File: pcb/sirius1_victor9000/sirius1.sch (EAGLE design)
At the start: 28 parts, among them IC3 STM32F042F4, SW1 324_SW, SW4 324_SW, U1 RJ45

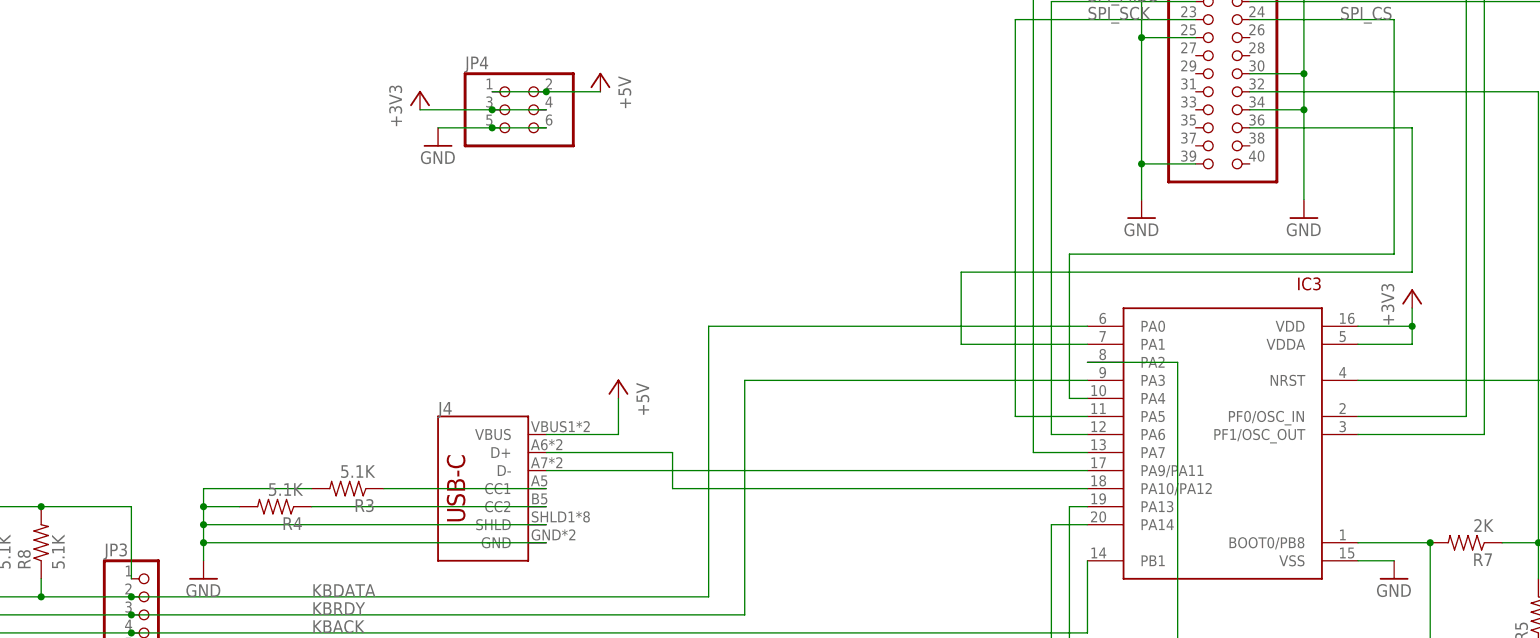
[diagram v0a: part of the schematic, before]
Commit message: added presence detection
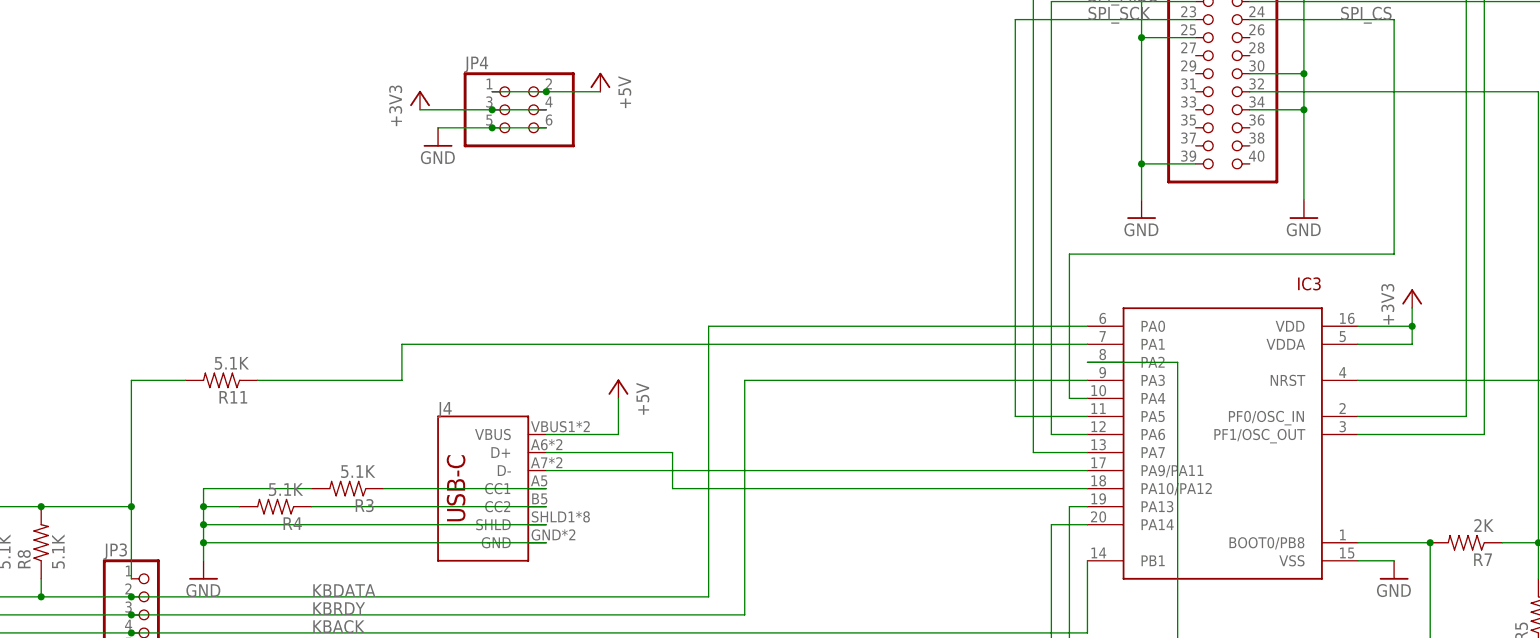
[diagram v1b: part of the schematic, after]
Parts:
- added R11: 5.1K, SparkFun-Passives:RESISTOR0805-RES
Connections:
- removed net N$12: IC3.PA1, JP1.36
- new net N$4: IC3.PA1, R11.1
- net N$27: now also R11.2
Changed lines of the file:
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@@
 <part name="JP3" library="pinhead" library_urn="urn:adsk.eagle:library:325" deviceset="PINHD-1X5" device="" package3d_urn="urn:adsk.eagle:package:22469/2"/>
 <part name="GND13" library="supply1" library_urn="urn:adsk.eagle:library:371" deviceset="GND" device=""/>
+<part name="R11" library="SparkFun-Passives" deviceset="RESISTOR" device="0805-RES" value="5.1K"/>
 </parts>
 <sheets>
@@
 <instance part="GND13" gate="1" x="-53.34" y="-142.24" smashed="yes">
 <attribute name="VALUE" x="-55.88" y="-144.78" size="1.778" layer="96"/>
+</instance>
+<instance part="R11" gate="G$1" x="-40.64" y="-96.52" smashed="yes" rot="R180">
+<attribute name="NAME" x="-36.83" y="-98.0186" size="1.778" layer="95" rot="R180"/>
+<attribute name="VALUE" x="-36.83" y="-93.218" size="1.778" layer="96" rot="R180"/>
 </instance>
 </instances>
@@
 </segment>
 </net>
-<net name="N$12" class="0">
-<segment>
-<pinref part="IC3" gate="G$1" pin="PA1"/>
-<wire x1="81.28" y1="-91.44" x2="63.5" y2="-91.44" width="0.1524" layer="91"/>
-<wire x1="63.5" y1="-91.44" x2="63.5" y2="-81.28" width="0.1524" layer="91"/>
-<wire x1="63.5" y1="-81.28" x2="127" y2="-81.28" width="0.1524" layer="91"/>
-<wire x1="127" y1="-81.28" x2="127" y2="-60.96" width="0.1524" layer="91"/>
-<pinref part="JP1" gate="A" pin="36"/>
-<wire x1="127" y1="-60.96" x2="104.14" y2="-60.96" width="0.1524" layer="91"/>
-</segment>
-</net>
 <net name="N$17" class="0">
 <segment>
@@
 <wire x1="-53.34" y1="-114.3" x2="-53.34" y2="-124.46" width="0.1524" layer="91"/>
 <junction x="-66.04" y="-114.3"/>
+<wire x1="-53.34" y1="-114.3" x2="-53.34" y2="-96.52" width="0.1524" layer="91"/>
+<wire x1="-53.34" y1="-96.52" x2="-45.72" y2="-96.52" width="0.1524" layer="91"/>
+<junction x="-53.34" y="-114.3"/>
+<pinref part="R11" gate="G$1" pin="2"/>
 </segment>
 </net>
@@
 </segment>
 </net>
+<net name="N$4" class="0">
+<segment>
+<pinref part="R11" gate="G$1" pin="1"/>
+<wire x1="-35.56" y1="-96.52" x2="-15.24" y2="-96.52" width="0.1524" layer="91"/>
+<pinref part="IC3" gate="G$1" pin="PA1"/>
+<wire x1="81.28" y1="-91.44" x2="-15.24" y2="-91.44" width="0.1524" layer="91"/>
+<wire x1="-15.24" y1="-91.44" x2="-15.24" y2="-96.52" width="0.1524" layer="91"/>
+</segment>
+</net>
